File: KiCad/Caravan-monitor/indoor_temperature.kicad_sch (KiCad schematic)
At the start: 3 parts

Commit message: Schematics done
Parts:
- C19: footprint Capacitor_SMD:C_0805_2012Metric_Pad1.18x1.45mm_HandSolder -> Capacitor_SMD:C_0402_1005Metric_Pad0.74x0.62mm_HandSolder
- R14, TH1: footprint Resistor_SMD:R_0805_2012Metric_Pad1.20x1.40mm_HandSolder -> Resistor_SMD:R_0402_1005Metric_Pad0.72x0.64mm_HandSolder
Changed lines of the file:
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@@
 			)
 		)
-		(property "Footprint" "Capacitor_SMD:C_0805_2012Metric_Pad1.18x1.45mm_HandSolder"
+		(property "Footprint" "Capacitor_SMD:C_0402_1005Metric_Pad0.74x0.62mm_HandSolder"
 			(at 159.7152 96.52 0)
 			(effects
@@
 			)
 		)
-		(property "Footprint" "Resistor_SMD:R_0805_2012Metric_Pad1.20x1.40mm_HandSolder"
+		(property "Footprint" "Resistor_SMD:R_0402_1005Metric_Pad0.72x0.64mm_HandSolder"
 			(at 138.43 93.98 0)
 			(effects
@@
 			)
 		)
-		(property "Footprint" "Resistor_SMD:R_0805_2012Metric_Pad1.20x1.40mm_HandSolder"
+		(property "Footprint" "Resistor_SMD:R_0402_1005Metric_Pad0.72x0.64mm_HandSolder"
 			(at 136.652 82.55 90)
 			(effects

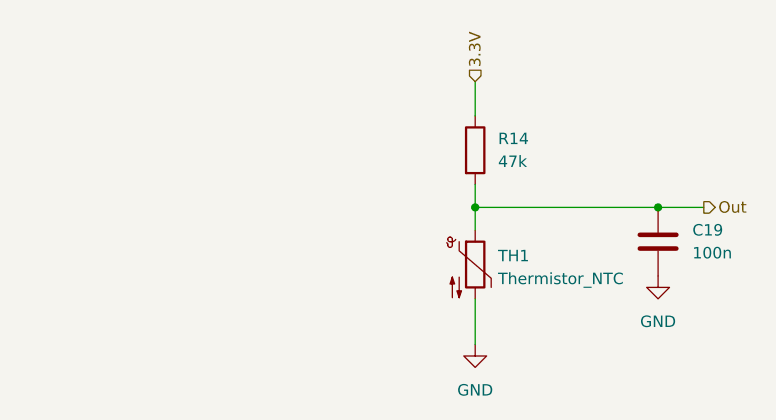
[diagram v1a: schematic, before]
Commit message: Schematic updates
Parts changed for JLCPCB assembly compatibility
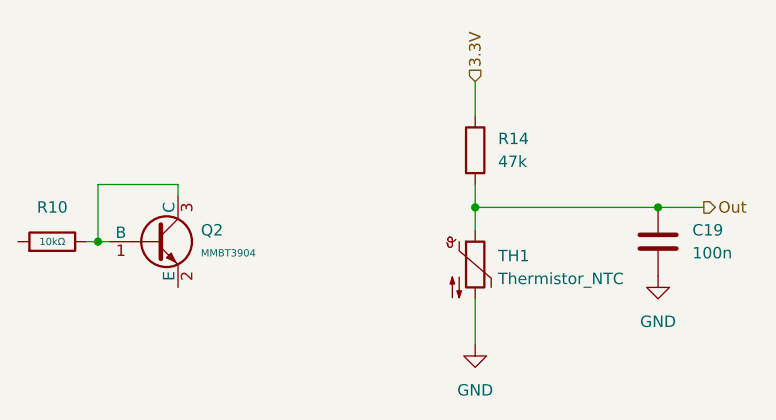
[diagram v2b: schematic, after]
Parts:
- added Q2: MMBT3904, PCM_JLCPCB:Q_SOT-23, symbol PCM_JLCPCB-Transistors:NPN,MMBT3904
- added R10: 10kΩ, PCM_JLCPCB:R_0402, symbol PCM_JLCPCB-Resistors:0402,10kΩ
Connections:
- new net: Q2.1 (B), Q2.3 (C), R10.2
